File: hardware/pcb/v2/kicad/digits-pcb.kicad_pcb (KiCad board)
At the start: 2 copper layers, 76.2 x 56.9 mm, 71 parts, among them J1 Conn_02x20_Odd_Even, J3 VIN_BARREL_PIGTAIL, J4 Conn_01x07, J6 Conn_01x02, J7 Screw_Terminal_01x02, J8 Conn_01x04, J9 Conn_01x03, SW1 SW_Push, U1 LM2596S-5, U2 DRV8871DDAR, U3 RP2040, U4 W25Q16JVSSIQ, U5 AMS1117-3.3, U6 TLV320AIC3104IRHBR, U7 XC6206P182MR, Y1 ABM8-272-T3

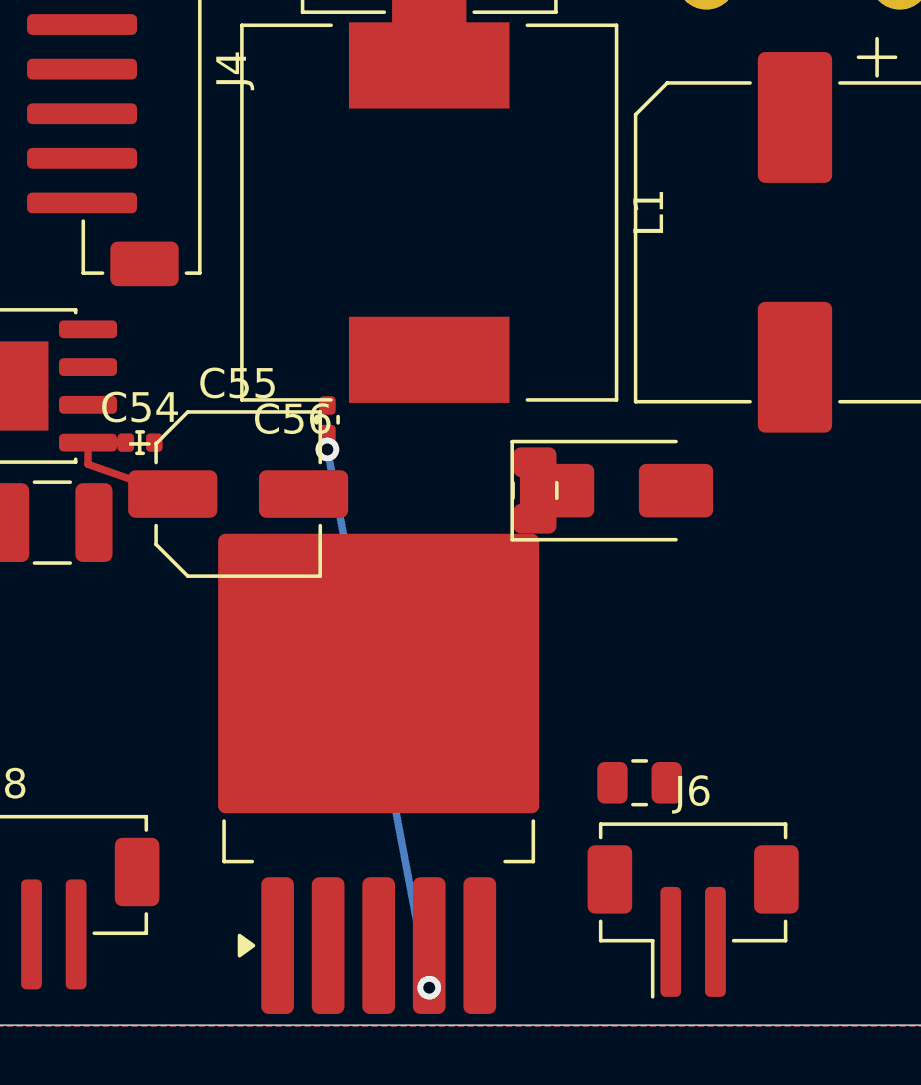
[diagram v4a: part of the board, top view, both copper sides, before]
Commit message: fix(hardware): correct check_decoupling rotation + fix buck cluster geometry
**Root cause**: check_decoupling.py's rotate() function used the wrong
rotation convention for KiCad. KiCad internally uses (x,y) -> (y, -x)
for +90 deg rotation; the script was using (x,y) -> (-y, x) which is
the opposite direction. This produced phantom "PASS" results for any
rotated footprint: pads were computed 180 deg from where KiCad DRC
actually sees them.

**Blast radius**: only footprints with rot != 0 were affected. Caps
(0402/0805) are symmetric, so the checker's wrong math and the right
math differ only in which pin is which side, not in distances. That's
why the codec and RP2040 clusters still passed. U1 (TO-263-5) is the
only IC with an asymmetric pin layout, and that's where the bug
mattered: the buck cluster was placed against check_decoupling's wrong
math, not against where KiCad actually thought U1's pin row was.

**Fix**:
- check_decoupling.py rotate() now matches KiCad's convention (with
  a comment explaining the gotcha).
- U1 rotated from +90 to -90 so pin row faces NORTH toward L1 (matching
  the cluster layout the user has in pcbnew).
- L1 rotated from -90 to +90 so pad 1 (SW_NODE) faces SOUTH toward
  U1.2 — the hot-loop pad is now on the correct side.
- D1 moved east 1mm (59.225 -> 60.225) to clear C4's footprint.
- C4 moved to (56, 49.5) rot=90 — C4 is actually an 0805 (2x1.25mm body)
  not 0402 as I had assumed, so its pad span (1.9mm) exceeds U1's pin
  pitch (1.7mm). Can't sit between pins; must offset diagonally.
- Deleted 2 stale F.Cu segments at (52.925, 68.685) and (52.925, 70.1)
  from the old wrong-rotation routing.
- buck_targets.json: D1 relaxed 7mm -> 8mm (need C4 clearance), C4
  relaxed 3mm -> 5mm (0805 footprint, not 0402) with rationale.

**Results**:
- check_buck_placement: 6/6 PASS.
- All other cluster checks still PASS.
- check_codec_subsheet / check_ringer_subsheet still PASS.
- copper_edge_clearance on U1 (5 violations) ELIMINATED.
- shorting_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
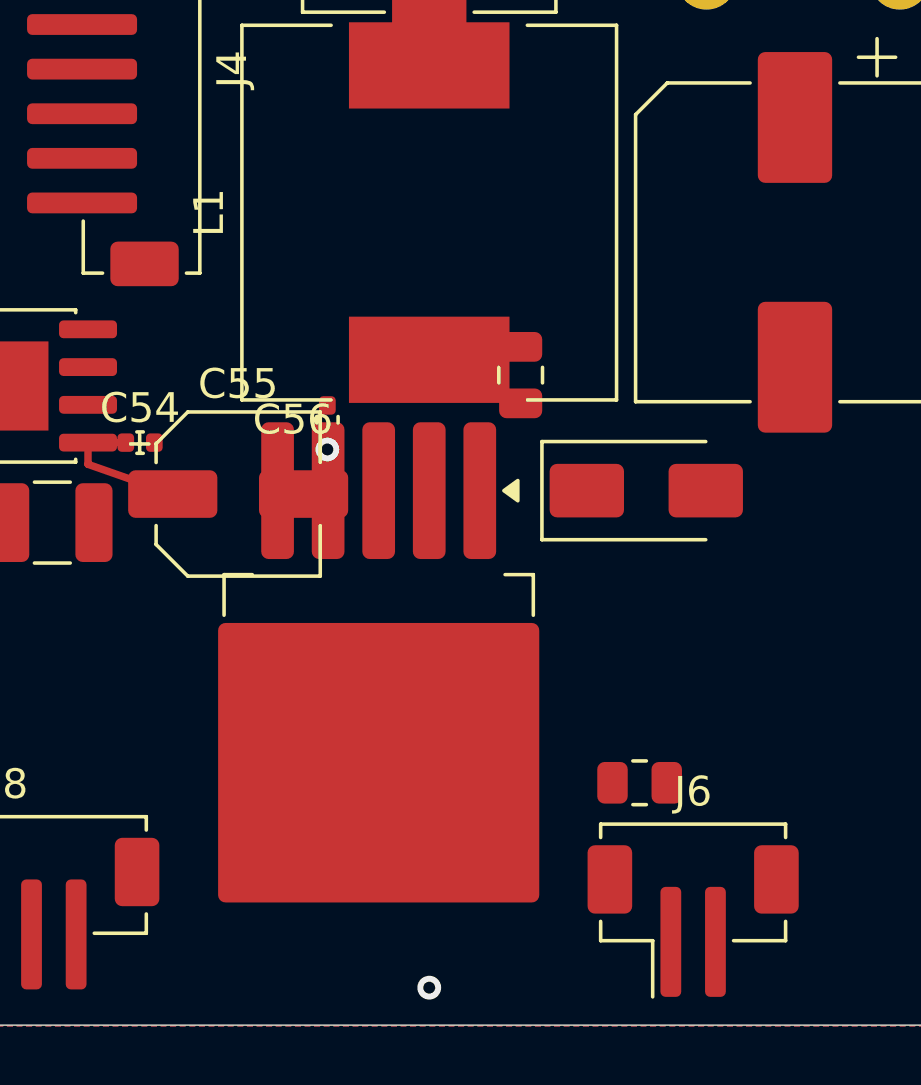
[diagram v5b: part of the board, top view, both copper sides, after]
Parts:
- moved C4 3.91 mm to (56.0, 49.5)
- moved D1 1.00 mm to (60.2, 53.4)
- turned L1 to 90 degrees
- turned U1 to -90 degrees
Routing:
- net +5V: track 20.4 -> 0.52 mm
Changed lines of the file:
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@@
 	(footprint "Capacitor_SMD:C_0805_2012Metric"
 		(layer "F.Cu")
-		(at 56.48 53.38 90)
+		(at 56 49.5 90)
 		(descr "Capacitor SMD 0805 (2012 Metric), square (rectangular) end terminal, IPC-7351 nominal, (Body size source: IPC-SM-782 page 76, https://www.pcb-3d.com/wordpress/wp-content/uploads/ipc-sm-782a_amendment_1_and_2.pdf, https://docs.google.com/spreadsheets/d/1BsfQQcO9C6DZCsRaXUlFlo91Tg2WpOkGARC1WS5S8t0/edit?usp=sharing)")
 		(tags "capacitor")
@@
 	(footprint "Diode_SMD:D_SMA"
 		(layer "F.Cu")
-		(at 59.225 53.385)
+		(at 60.225 53.385)
 		(descr "Diode SMA (DO-214AC)")
 		(tags "Diode SMA (DO-214AC)")
@@
 	(footprint "Package_TO_SOT_SMD:TO-263-5_TabPin3"
 		(layer "F.Cu")
-		(at 51.225 61.035 90)
+		(at 51.225 61.035 -90)
 		(descr "TO-263/D2PAK/DDPAK SMD package, http://www.infineon.com/cms/en/product/packages/PG-TO263/PG-TO263-5-1/")
 		(tags "D2PAK DDPAK TO-263 D2PAK-5 TO-263-5 SOT-426")
@@
 	(footprint "Inductor_SMD:L_12x12mm_H8mm"
 		(layer "F.Cu")
-		(at 52.925 44.035 -90)
+		(at 52.925 44.035 90)
 		(descr "Choke, SMD, 12x12mm 8mm height")
 		(tags "Choke SMD")
@@
 	)
 	(segment
-		(start 52.925 68.685)
-		(end 52.925 70.1)
-		(width 0.25)
-		(layer "F.Cu")
-		(net "+5V")
-		(locked yes)
-	)
-	(segment
 		(start 49.5 52)
 		(end 49.5 51.48)
@@
 		(net "+5V")
 		(locked yes)
-	)
-	(segment
-		(start 52.925 70.1)
-		(end 49.5 52)
-		(width 0.25)
-		(layer "B.Cu")
-		(net "+5V")
-		(locked yes)

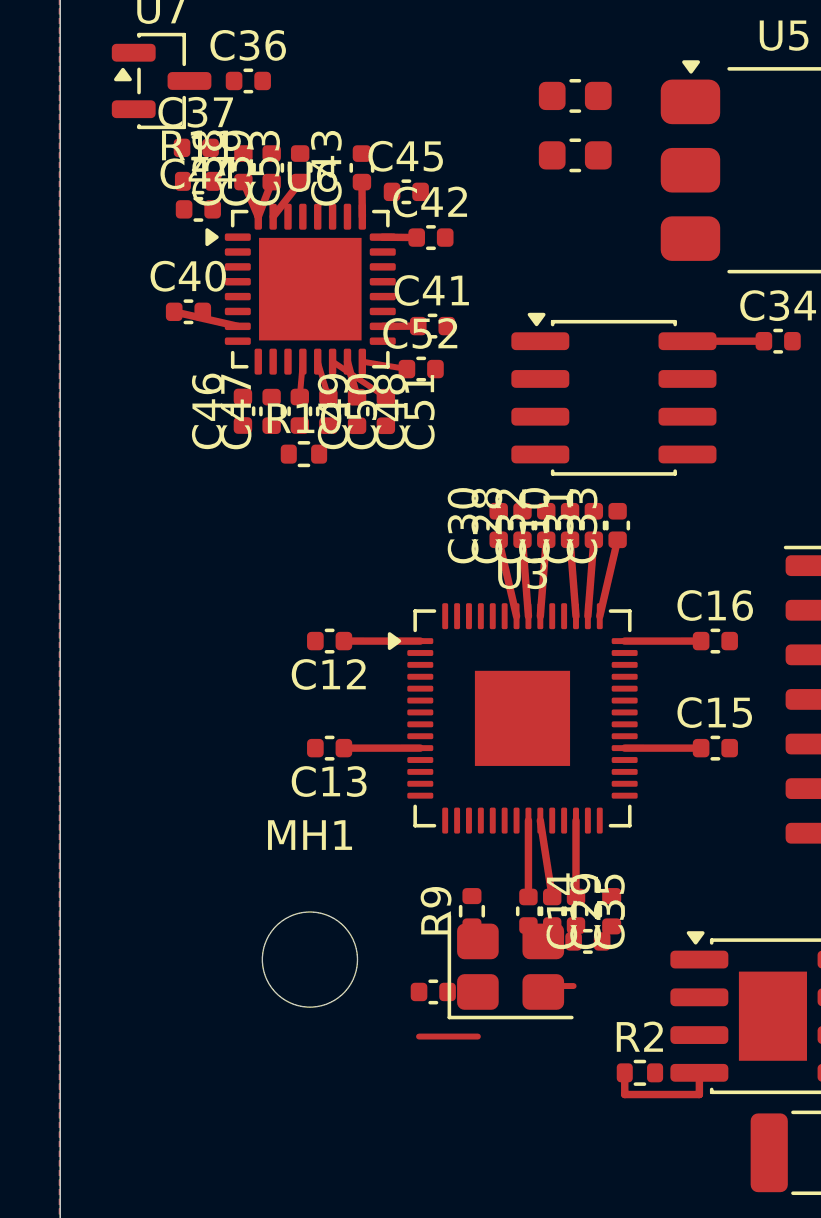
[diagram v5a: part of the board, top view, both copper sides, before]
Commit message: fix(hardware): remove 3 stale/dangling traces after rotation fix
- XIN dangling trace at (29.05, 50.55) -> (27.07, 50.55). Left over
  from when Y1/C5/C6 got shifted 1.5mm north earlier in the session;
  the trace didn't move with them.
- Old CODEC_RESET trace that was brushing U6 pin 30 (reason for the
  track-vs-pad short reported in earlier DRC runs). Deleted. An attempt
  to reroute it as an L-path hit C39's +1V8 pad instead, so the trace
  is now unrouted entirely - user will re-route manually.

Real DRC issues: 87 -> 84. Still need supervised cleanup for the
crystal cluster shorts and the remaining buck-cluster courtyards.
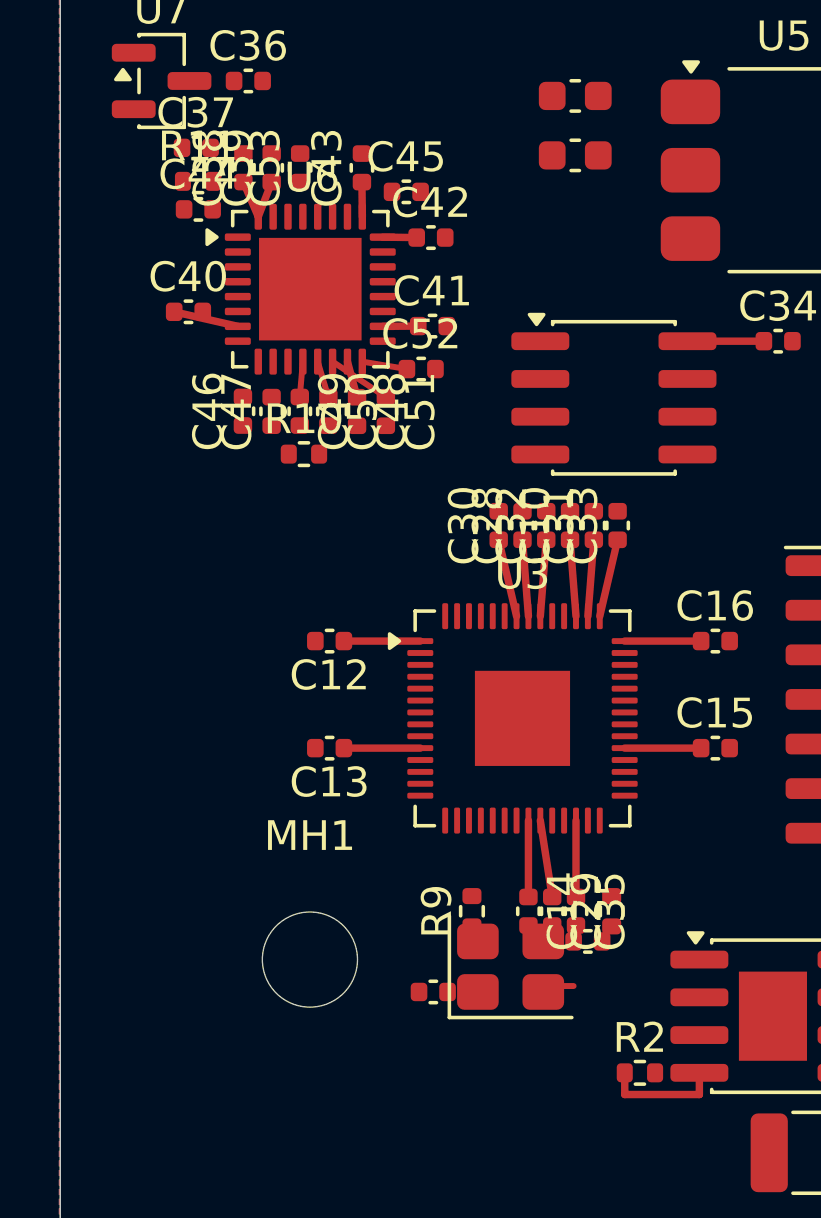
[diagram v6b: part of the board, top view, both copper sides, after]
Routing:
- net XIN: track 1.98 -> 0.00 mm
- net CODEC_RESET: track 1.48 -> 0.00 mm
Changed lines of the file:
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@@
-	)
-	(segment
-		(start 22.1625 22.9725)
-		(end 23.0711 21.8081)
-		(width 0.25)
-		(locked yes)
-		(layer "F.Cu")
-		(net "CODEC_RESET")
-	)
-	(segment
-		(start 29.05 50.55)
-		(end 27.07 50.55)
-		(width 0.2)
-		(locked yes)
-		(layer "F.Cu")
-		(net "XIN")
 	)
 	(segment

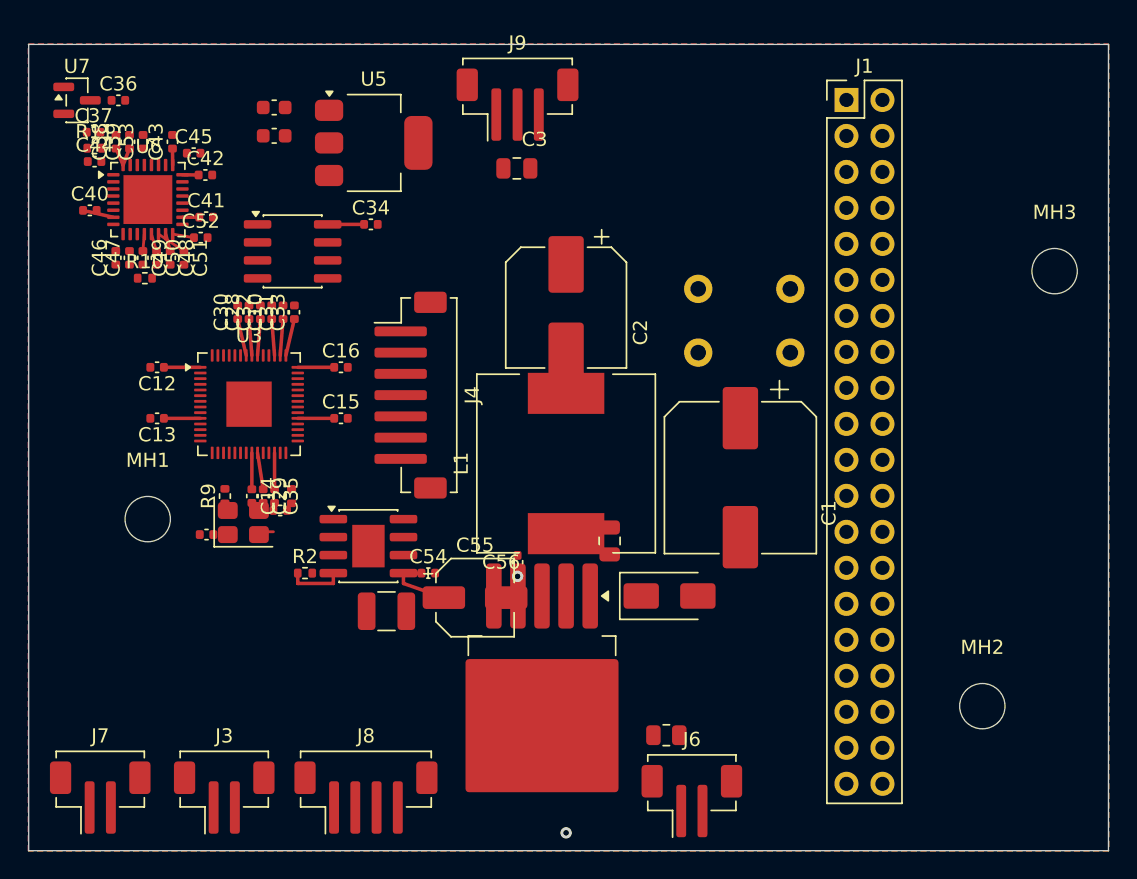
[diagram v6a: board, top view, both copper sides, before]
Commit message: feat(hardware): TI-reference buck spine placement, full cluster realignment
Buck cluster rebuilt to match LM2596 datasheet Fig 9-13 (ramuroy reference):
linear C1 - U1 - D1 - L1 - C2 east-west spine with D1 tucked under U1.2
and nothing between U1 and L1. buck_targets.json updated with physical
minimums derived from actual footprint geometry (12x12 L1 next to 11.3mm
U1 courtyard = 15mm floor for L1-to-U1.2 center distance).

Placement checkers all pass (50/50 constraints):
  buck 6/6, codec 20/20, crystal 3/3, flash 2/2, LDO 2/2,
  ringer 3/3, RP2040 decoupling 14/14.

Real DRC down from 79 to 9 issues (3 clearance + 6 courtyard_overlap),
all concentrated at the RP2040 +3V3/DVDD_1V1 decoupling corner (C10
vs C28/C30/C31/C32 pad-to-pad 0.18mm vs 0.20mm Power netclass floor)
and one harmless same-net C56/C2 courtyard touch on +5V.

Removed duplicate C5/C6 entries from decoupling_targets.json that
conflicted with the crystal_targets.json allow_body_overlap constraint.
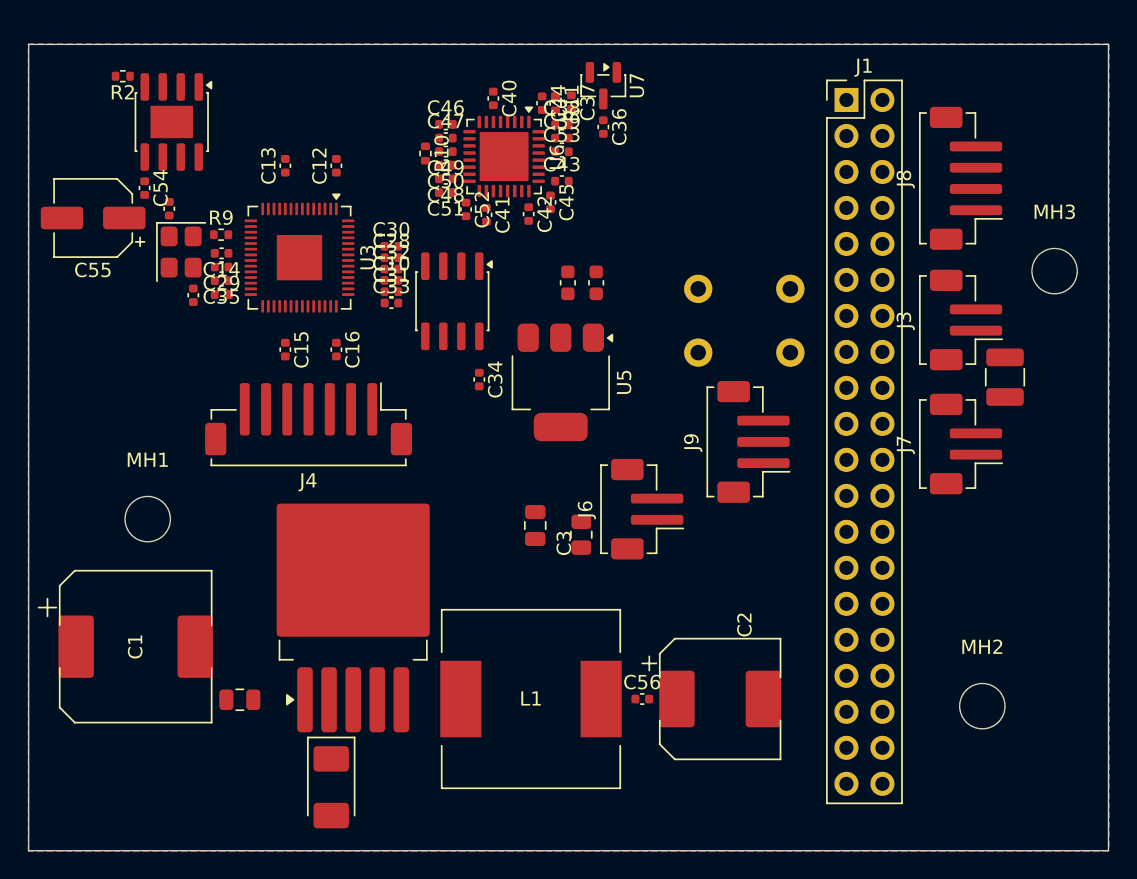
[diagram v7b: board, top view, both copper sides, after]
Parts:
- moved J7 66.0 mm to (81.2, 42.7), turned to 90 degrees
- moved J3 62.3 mm to (81.2, 33.9), turned to 90 degrees
- moved J8 60.9 mm to (81.2, 23.9), turned to 90 degrees
- moved F1 46.7 mm to (83.9, 37.9), turned to -90 degrees
- moved C1 44.3 mm to (22.6, 57.0), turned to 0 degrees
- moved C55 38.0 mm to (19.6, 26.7), turned to 180 degrees
- moved R2 37.3 mm to (21.6, 16.7), turned to 180 degrees
- moved U7 37.2 mm to (55.6, 17.4), turned to -90 degrees
- moved C36 34.3 mm to (55.6, 20.3), turned to -90 degrees
- moved C37 33.8 mm to (53.3, 18.5), turned to -90 degrees
- moved C54 33.8 mm to (23.2, 24.6), turned to -90 degrees
- moved U2 33.0 mm to (25.1, 19.9), turned to -90 degrees
- moved R11 32.7 mm to (52.2, 18.6), turned to -90 degrees
- moved C44 31.9 mm to (51.2, 18.6), turned to -90 degrees
- moved C38 31.5 mm to (52.6, 20.1), turned to 0 degrees
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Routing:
- net +3V3: track 31.5 -> 0.00 mm
- net DVDD_1V1: track 7.82 -> 0.00 mm
- net +12V: track 5.02 -> 0.00 mm
- net ILIM: track 3.97 -> 0.00 mm
- net RUN: track 2.57 -> 0.00 mm
- net /codec/+1V8: track 2.52 -> 0.00 mm
- net /codec/MIC2L_INT: track 2.15 -> 0.00 mm
- net /codec/MIC2R_INT: track 1.52 -> 0.00 mm
- net /codec/MIC1RM_INT: track 1.25 -> 0.00 mm
- net /codec/MICBIAS: track 1.24 -> 0.00 mm
- net /codec/MIC1RP_INT: track 1.19 -> 0.00 mm
- net GND: track 1.02 -> 0.00 mm
- net +5V: track 0.52 -> 0.00 mm, vias 2 -> 0
